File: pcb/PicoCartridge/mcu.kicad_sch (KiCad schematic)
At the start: 42 parts, among them J301 DBG, SW301 SW_Push, SW302 SW_Push, U1 RP2350B-QFN80, U2 W25Q128JVS, U3 MCP7940N-xSN, Y301 Crystal_GND24, Y302 Crystal

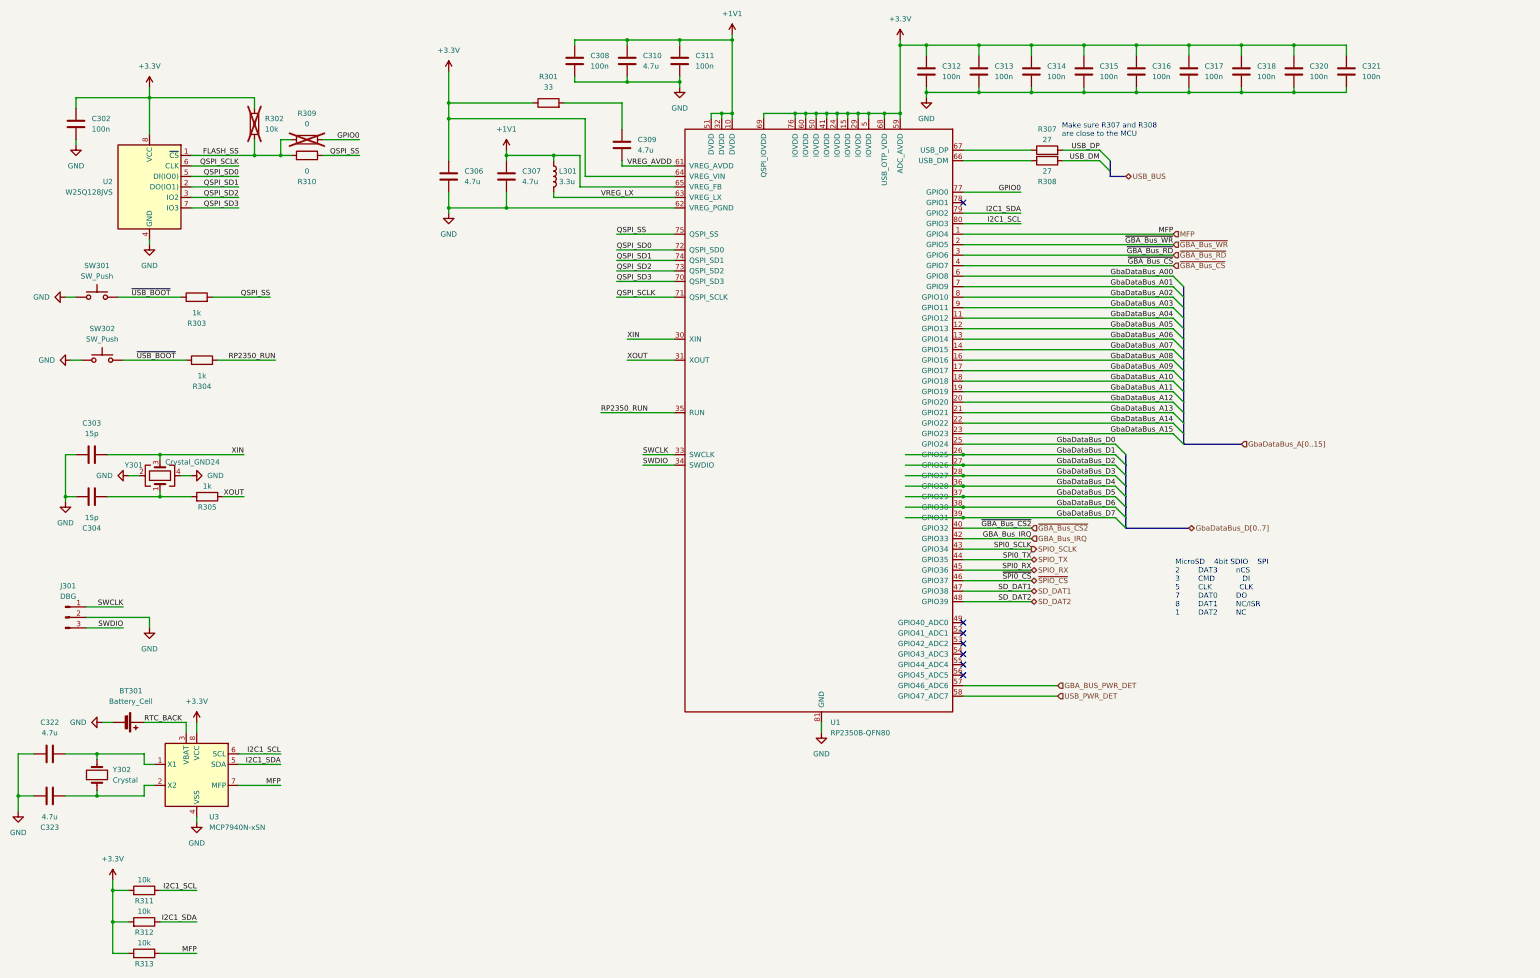
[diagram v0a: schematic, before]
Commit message: Added programmer connection (#4)
* Removed dedicated usb connector

Use would be very limited (live view on a pc and data transfer without
removing the sd card) and increases the pcb & schematic complexity by a lot.

Removing the usb connector for this revision. It is possible, if this design
is successful that I will create a new revision at some point. You never know.

* Added programmer "connector"

Additionally removed reset and program switches as there is no need for
them on the pcb itself if there is no usb connection.
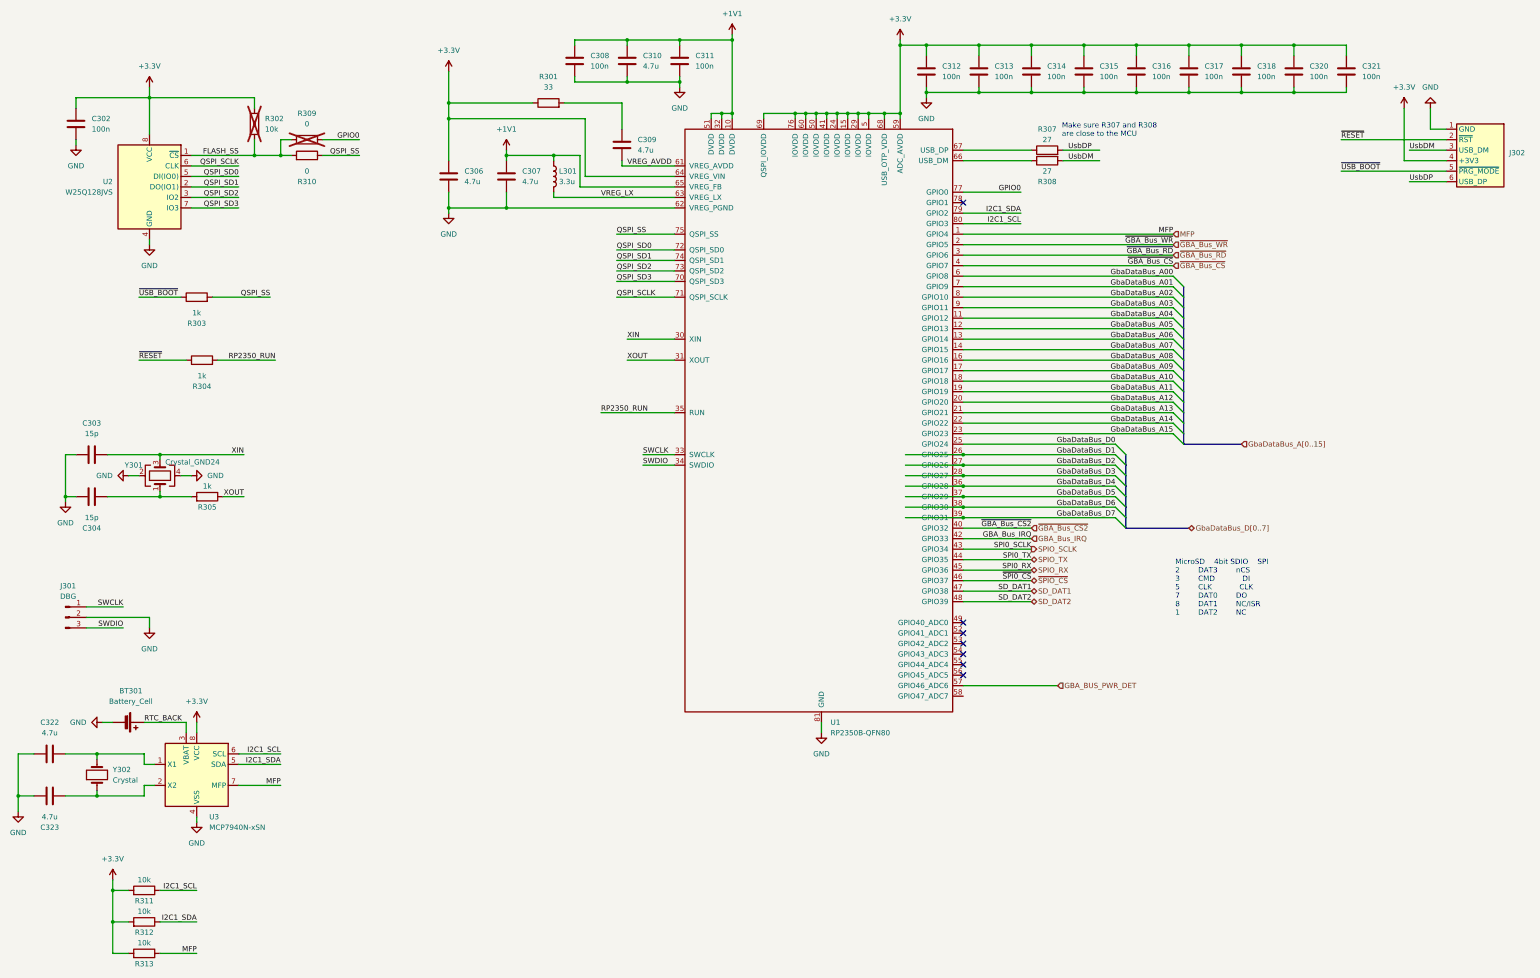
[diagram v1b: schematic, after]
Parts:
- removed SW301, SW302: SW_Push, symbol Switch:SW_Push
- added J302: ~, PicoCartridge:ProgrammerConnector_SMD, symbol PicoCartridge:Programmer
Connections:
- net +3.3V: now also J302.4 (+3V3)
- net GND: now also J302.1 (GND)
- net ~{USB_BOOT}: now also J302.5 (~{PRG_MODE}); no longer R304.1
- net USB_DM renamed UsbDM
- net UsbDM: now also J302.3 (USB_DM)
- net USB_DP renamed UsbDP
- net UsbDP: now also J302.6 (USB_DP)
- net USB_PWR_DET: no longer names the net of U1.58 (GPIO47_ADC7)
- new net ~{RESET}: J302.2 (~{RST}), R304.1
